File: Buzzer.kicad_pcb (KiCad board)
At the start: 4 copper layers, 70 x 90 mm, 57 parts, among them J1 AudioJack2_Ground, J2 AVR-ISP-6, J3 Screw_Terminal_01x07, J4 Screw_Terminal_01x02, J5 Screw_Terminal_01x02, J6 Screw_Terminal_01x02, J7 Screw_Terminal_01x02, J8 USB-C-Board, Q1 BC547, Q2 BC547, Q3 BC547, Q4 BC547, Q5 BC547, SW1 SW_Reset, SW2 SW_Next, SW3 SW_New, U1 ATmega328-P, U2 HDSP-7401, Y1 16 (or 20) MHz

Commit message: Add revision 2 circuit, pcb and documentation.
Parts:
- removed D6: Rot, LED_THT:LED_Rectangular_W3.9mm_H1.8mm
- removed D7: Grün, LED_THT:LED_Rectangular_W3.9mm_H1.8mm
- removed Q1, Q2, Q3, Q4, Q5: BC547, Package_TO_SOT_THT:TO-92_Inline_Wide
- added C13: 47u, Capacitor_THT:CP_Radial_D8.0mm_P3.50mm, F.Cu at (124.5, 53.3)
- added C14: 100n, Capacitor_THT:C_Disc_D5.0mm_W2.5mm_P2.50mm, F.Cu at (129.5, 97.8)
- added C15: 100n, Capacitor_THT:C_Disc_D5.0mm_W2.5mm_P2.50mm, F.Cu at (129.5, 109.2)
- added C16: 100n, Capacitor_THT:C_Disc_D5.0mm_W2.5mm_P2.50mm, F.Cu at (129.5, 120.6)
- added C17: 100n, Capacitor_THT:C_Disc_D5.0mm_W2.5mm_P2.50mm, F.Cu at (144.7, 57.0)
- added C18: 220n, Capacitor_THT:C_Disc_D5.0mm_W2.5mm_P2.50mm, F.Cu at (134.7, 57.0)
- added C19: 100n, Capacitor_THT:C_Disc_D5.0mm_W2.5mm_P2.50mm, F.Cu at (188.0, 33.0)
- added C20: 100n, Capacitor_THT:C_Disc_D5.0mm_W2.5mm_P2.50mm, F.Cu at (182.9, 35.6)
- added C21: 100n, Capacitor_THT:C_Disc_D5.0mm_W2.5mm_P2.50mm, F.Cu at (170.2, 96.5)
- added D_{Buzz}1: LED_Small, LED_THT:LED_Rectangular_W5.0mm_H2.0mm, F.Cu at (248.9, 81.3)
- added D_{Power}1: LED_Small, LED_THT:LED_Rectangular_W5.0mm_H2.0mm, F.Cu at (243.8, 81.3)
- added D_{P}1: LED_Small, LED_THT:LED_Rectangular_W5.0mm_H2.0mm, F.Cu at (203.2, 132.2)
- added D_{P}2: LED_Small, LED_THT:LED_Rectangular_W5.0mm_H2.0mm, F.Cu at (208.3, 132.2)
- added D_{P}3: LED_Small, LED_THT:LED_Rectangular_W5.0mm_H2.0mm, F.Cu at (213.4, 132.2)
- added D_{P}4: LED_Small, LED_THT:LED_Rectangular_W5.0mm_H2.0mm, F.Cu at (218.4, 132.1)
- added D_{P}5: LED_Small, LED_THT:LED_Rectangular_W5.0mm_H2.0mm, F.Cu at (223.5, 132.1)
- added D_{P}6: LED_Small, LED_THT:LED_Rectangular_W5.0mm_H2.0mm, F.Cu at (228.6, 132.1)
- added D_{RX}1: LED_Small, LED_THT:LED_Rectangular_W5.0mm_H2.0mm, F.Cu at (256.5, 81.3)
- added D_{Ready}1: LED_Small, LED_THT:LED_Rectangular_W5.0mm_H2.0mm, F.Cu at (193.0, 132.1)
- added D_{TX}1: LED_Small, LED_THT:LED_Rectangular_W5.0mm_H2.0mm, F.Cu at (261.6, 81.3)
- added G***: LOGO, LOGO, F.Cu at (259.1, 49.5)
- added G***: LOGO, LOGO, F.Cu at (241.3, 38.1)
- added G***: LOGO, LOGO, F.Cu at (165.1, 83.8)
- added G***: LOGO, LOGO, B.Cu at (223.5, 33.0)
- added J10: Barrel_Jack, Connector_BarrelJack:BarrelJack_Kycon_KLDX-0202-xC_Horizontal, F.Cu at (127.0, 42.4)
- added J11: Screw_Terminal_01x10, TerminalBlock_Phoenix:TerminalBlock_Phoenix_MKDS-1,5-10-5.08_1x10_P5.08mm_Horizontal, F.Cu at (261.6, 147.3)
- added J12: Conn_01x03_Pin, Connector_PinHeader_2.54mm:PinHeader_1x03_P2.54mm_Vertical, F.Cu at (185.4, 48.3)
- added J13: Screw_Terminal_01x03, TerminalBlock_Phoenix:TerminalBlock_Phoenix_MKDS-1,5-3-5.08_1x03_P5.08mm_Horizontal, F.Cu at (160.0, 33.0)
- added J9: USB_B, Connector_USB:USB_B_OST_USB-B1HSxx_Horizontal, F.Cu at (170.2, 43.4)
- added JP2: USB Reset, Connector_PinHeader_2.54mm:PinHeader_1x03_P2.54mm_Vertical, F.Cu at (188.0, 63.5)
- added JP3: USB-UART, Connector_PinHeader_2.54mm:PinHeader_1x03_P2.54mm_Vertical, F.Cu at (190.5, 48.3)
- added R17: 220-1k, Resistor_THT:R_Axial_DIN0207_L6.3mm_D2.5mm_P10.16mm_Horizontal, F.Cu at (218.4, 137.2)
- added R18: 220-1k, Resistor_THT:R_Axial_DIN0207_L6.3mm_D2.5mm_P10.16mm_Horizontal, F.Cu at (223.5, 137.2)
- added R19: 220-1k, Resistor_THT:R_Axial_DIN0207_L6.3mm_D2.5mm_P10.16mm_Horizontal, F.Cu at (228.6, 137.2)
- added R20: 220-1k, Resistor_THT:R_Axial_DIN0207_L6.3mm_D2.5mm_P10.16mm_Horizontal, F.Cu at (261.6, 63.5)
- added R21: 220-1k, Resistor_THT:R_Axial_DIN0207_L6.3mm_D2.5mm_P10.16mm_Horizontal, F.Cu at (256.5, 63.5)
- added R22: 220-1k, Resistor_THT:R_Axial_DIN0207_L6.3mm_D2.5mm_P10.16mm_Horizontal, F.Cu at (248.9, 63.5)
- added R23: 220-1k, Resistor_THT:R_Axial_DIN0207_L6.3mm_D2.5mm_P10.16mm_Horizontal, F.Cu at (243.8, 63.5)
- added R24: 10k, Resistor_THT:R_Axial_DIN0207_L6.3mm_D2.5mm_P7.62mm_Horizontal, F.Cu at (152.4, 86.4)
- added R25: 10k, Resistor_THT:R_Axial_DIN0207_L6.3mm_D2.5mm_P10.16mm_Horizontal, F.Cu at (147.3, 88.9)
- added R26: 10k, Resistor_THT:R_Axial_DIN0207_L6.3mm_D2.5mm_P15.24mm_Horizontal, F.Cu at (142.2, 94.0)
- added R27: 10k, Resistor_THT:R_Axial_DIN0207_L6.3mm_D2.5mm_P15.24mm_Horizontal, F.Cu at (142.2, 106.7)
- added R28: 10k, Resistor_THT:R_Axial_DIN0207_L6.3mm_D2.5mm_P10.16mm_Horizontal, F.Cu at (147.3, 111.8)
- added R29: 10k, Resistor_THT:R_Axial_DIN0207_L6.3mm_D2.5mm_P7.62mm_Horizontal, F.Cu at (152.4, 114.3)
- added R30: 10k, Resistor_THT:R_Axial_DIN0207_L6.3mm_D2.5mm_P10.16mm_Horizontal, F.Cu at (180.3, 134.6)
- added R31: 10k, Resistor_THT:R_Axial_DIN0207_L6.3mm_D2.5mm_P10.16mm_Horizontal, F.Cu at (160.0, 134.6)
- added REF**: WEEE-Logo_5.6x8mm_SilkScreen, Symbol:WEEE-Logo_5.6x8mm_SilkScreen, F.Cu at (123.8, 152.4)
- added REF**: OSHW-Symbol_6.7x6mm_SilkScreen, Symbol:OSHW-Symbol_6.7x6mm_SilkScreen, F.Cu at (132.1, 152.4)
- added REF**: MountingHole_2.7mm_M2.5_ISO7380_Pad, MountingHole:MountingHole_2.7mm_M2.5_ISO7380_Pad, F.Cu at (116.8, 31.6)
- added REF**: MountingHole_2.7mm_M2.5_ISO7380_Pad, MountingHole:MountingHole_2.7mm_M2.5_ISO7380_Pad, F.Cu at (264.1, 153.9)
- added REF**: MountingHole_2.7mm_M2.5_ISO7380_Pad, MountingHole:MountingHole_2.7mm_M2.5_ISO7380_Pad, F.Cu at (116.8, 153.9)
- added REF**: MountingHole_2.7mm_M2.5_ISO7380_Pad, MountingHole:MountingHole_2.7mm_M2.5_ISO7380_Pad, F.Cu at (264.1, 31.6)
- added REF**: Symbol_Barrel_Polarity, Symbol:Symbol_Barrel_Polarity, B.Cu at (127.0, 30.5)
- added REF**: Smolhaj_Scale_0.1, Symbol:Smolhaj_Scale_0.1, B.Cu at (266.0, 39.5)
- added U3: 74HC4051, Package_DIP:DIP-16_W7.62mm_Socket, F.Cu at (213.4, 104.1)
- added U4: 4511, Package_DIP:DIP-16_W7.62mm_Socket, F.Cu at (205.7, 53.3)
- added U5: CH340C, Package_SO:SOIC-16_3.9x9.9mm_P1.27mm, F.Cu at (189.2, 40.0)
- added U6: L7805, Package_TO_SOT_THT:TO-220-3_Horizontal_TabDown, F.Cu at (137.2, 53.3)
- added U7: 74LS07, Package_DIP:DIP-14_W7.62mm_Socket, F.Cu at (246.4, 149.9)
- added U8: 74LS07, Package_DIP:DIP-14_W7.62mm_Socket, F.Cu at (238.8, 88.9)
- C1, C4: footprint Capacitor_THT:CP_Radial_D10.0mm_P2.50mm -> Capacitor_THT:CP_Radial_D6.3mm_P2.50mm
- C10, C11, C12, C7, C8, C9: value 10n -> 100n; footprint Capacitor_THT:C_Disc_D3.0mm_W1.6mm_P2.50mm -> Capacitor_THT:C_Disc_D5.0mm_W2.5mm_P2.50mm
- C2, C3: footprint Capacitor_THT:C_Disc_D3.0mm_W1.6mm_P2.50mm -> Capacitor_THT:C_Disc_D5.0mm_W2.5mm_P5.00mm
- C5, C6: footprint Capacitor_THT:C_Disc_D3.0mm_W1.6mm_P2.50mm -> Capacitor_THT:C_Disc_D5.0mm_W2.5mm_P2.50mm
- D1, D5: value Rot -> SR104; footprint LED_THT:LED_Rectangular_W3.9mm_H1.8mm -> Diode_THT:D_DO-41_SOD81_P7.62mm_Horizontal
- D2: value BAT85 -> SR104; footprint Diode_THT:D_T-1_P5.08mm_Horizontal -> Diode_THT:D_DO-41_SOD81_P7.62mm_Horizontal
- D3: value BAT85 -> SR104; footprint Diode_THT:D_T-1_P5.08mm_Horizontal -> Diode_THT:D_DO-41_SOD81_P12.70mm_Horizontal
- D4: value Rot -> 1N4001; footprint LED_THT:LED_Rectangular_W3.9mm_H1.8mm -> Diode_THT:D_DO-41_SOD81_P7.62mm_Horizontal
- J1: value AudioJack2_Ground -> AudioJack3; footprint Connector_Audio:Jack_3.5mm_CUI_SJ1-3523N_Horizontal -> Connector_Audio:Jack_3.5mm_Ledino_KB3SPRS_Horizontal
- J3: value Screw_Terminal_01x07 -> Player 1; footprint TerminalBlock_Phoenix:TerminalBlock_Phoenix_MPT-0,5-7-2.54_1x07_P2.54mm_Horizontal -> TerminalBlock_Phoenix:TerminalBlock_Phoenix_MKDS-1,5-2-5.08_1x02_P5.08mm_Horizontal
- J4: value Screw_Terminal_01x02 -> Player 2; footprint TerminalBlock_Phoenix:TerminalBlock_Phoenix_MPT-0,5-2-2.54_1x02_P2.54mm_Horizontal -> TerminalBlock_Phoenix:TerminalBlock_Phoenix_MKDS-1,5-2-5.08_1x02_P5.08mm_Horizontal
- J5: value Screw_Terminal_01x02 -> Player 3; footprint TerminalBlock_Phoenix:TerminalBlock_Phoenix_MPT-0,5-2-2.54_1x02_P2.54mm_Horizontal -> TerminalBlock_Phoenix:TerminalBlock_Phoenix_MKDS-1,5-2-5.08_1x02_P5.08mm_Horizontal
- J6: value Screw_Terminal_01x02 -> Player 4; footprint TerminalBlock_Phoenix:TerminalBlock_Phoenix_MPT-0,5-2-2.54_1x02_P2.54mm_Horizontal -> TerminalBlock_Phoenix:TerminalBlock_Phoenix_MKDS-1,5-2-5.08_1x02_P5.08mm_Horizontal
- J7: value Screw_Terminal_01x02 -> Player 5; footprint TerminalBlock_Phoenix:TerminalBlock_Phoenix_MPT-0,5-2-2.54_1x02_P2.54mm_Horizontal -> TerminalBlock_Phoenix:TerminalBlock_Phoenix_MKDS-1,5-2-5.08_1x02_P5.08mm_Horizontal
- J8: value USB-C-Board -> Player 6; footprint Connector_PinHeader_2.54mm:PinHeader_1x06_P2.54mm_Horizontal -> TerminalBlock_Phoenix:TerminalBlock_Phoenix_MKDS-1,5-2-5.08_1x02_P5.08mm_Horizontal
- JP1: footprint Connector_PinHeader_2.54mm:PinHeader_1x02_P2.54mm_Vertical -> Connector_PinHeader_2.54mm:PinHeader_1x03_P2.54mm_Vertical
- R1, R10, R11, R2, R3, R4, R5, R6, R7, R8, R9: footprint Resistor_THT:R_Axial_DIN0204_L3.6mm_D1.6mm_P5.08mm_Horizontal -> Resistor_THT:R_Axial_DIN0207_L6.3mm_D2.5mm_P10.16mm_Horizontal
- R12: value 680 -> 10k; footprint Resistor_THT:R_Axial_DIN0204_L3.6mm_D1.6mm_P5.08mm_Horizontal -> Resistor_THT:R_Axial_DIN0207_L6.3mm_D2.5mm_P10.16mm_Horizontal
- R13, R14, R15, R16: value 680 -> 220-1k; footprint Resistor_THT:R_Axial_DIN0204_L3.6mm_D1.6mm_P5.08mm_Horizontal -> Resistor_THT:R_Axial_DIN0207_L6.3mm_D2.5mm_P10.16mm_Horizontal
- U1: value ATmega328-P -> ATmega328P-P; footprint Package_DIP:DIP-28_W7.62mm -> Package_DIP:DIP-28_W7.62mm_Socket
- U2: value HDSP-7401 -> HDSP-7803; footprint Display_7Segment:D1X8K -> Display_7Segment:HDSP-7801
- Y1: footprint Crystal:Resonator-2Pin_W7.0mm_H2.5mm -> Crystal:Crystal_HC49-U_Vertical
- moved U2 208.7 mm to (226.1, 66.0)
- moved R8 201.9 mm to (238.8, 45.7), turned to -90 degrees
- moved R4 199.2 mm to (238.8, 81.3), turned to 90 degrees
- moved R5 193.9 mm to (233.7, 81.3), turned to 90 degrees
- moved R3 193.5 mm to (233.7, 45.7), turned to -90 degrees
- moved R2 188.2 mm to (228.6, 45.7), turned to -90 degrees
- moved R7 188.0 mm to (228.6, 81.3), turned to 90 degrees
- moved R1 183.0 mm to (223.5, 45.7), turned to -90 degrees
- moved R6 182.9 mm to (223.5, 81.3), turned to 90 degrees
- moved R16 158.1 mm to (213.4, 137.2), turned to -90 degrees
- moved C5 149.9 mm to (190.5, 99.1), turned to 180 degrees
- moved R15 147.0 mm to (208.3, 137.2)
- moved SW3 147.0 mm to (184.1, 124.5), turned to -90 degrees
- moved SW1 144.1 mm to (172.7, 73.7)
- moved R14 140.6 mm to (203.2, 137.2), turned to -90 degrees
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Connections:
- net MOSI renamed Net-(J2-MOSI)
- C10 pad 1: Net-(J7-Pin_1) -> /PD4
- C7 pad 1: Net-(J4-Pin_1) -> Net-(U5-~{RTS})
- C7 pad 2: GND -> Net-(JP2-A)
- C8 pad 1: Net-(J5-Pin_1) -> /PD2
- C9 pad 1: Net-(J6-Pin_1) -> /PD3
- D1 pad 1: Net-(D1-K) -> /V_unfused
- D1 pad 2: Net-(D1-A) -> V_BARREL
- D2 pad 1: Net-(D2-K) -> /V_unfused
- D3 pad 1: Net-(D2-K) -> /V_unfused
- D4 pad 1: Net-(D4-K) -> /bjd
- D4 pad 2: SCK -> /bj
- D5 pad 1: Net-(D5-K) -> /V_unfused
- D5 pad 2: MISO -> V_SCREW
- F1 pad 1: Net-(D2-K) -> /V_unfused
- J1 pad R: (no net) -> Net-(C1-Pad2)
- J1 pad S: GND -> Net-(C1-Pad2)
- J1 pad T: Net-(C1-Pad2) -> GND
- J2 pad 1: MISO -> Net-(J2-MISO)
- J2 pad 3: SCK -> SCK / Buzzer
- J3 pad 1: +5V -> /PD2
- J3 pad 2: Net-(J3-Pin_2) -> GND
- J4 pad 1: Net-(J4-Pin_1) -> /PD3
- J5 pad 1: Net-(J5-Pin_1) -> /PD4
- J6 pad 1: Net-(J6-Pin_1) -> /PD5
- J7 pad 1: Net-(J7-Pin_1) -> /PD6
- J8 pad 1: unconnected-(J8-Pin_1-Pad1) -> /PD7
- J8 pad 2: unconnected-(J8-Pin_2-Pad2) -> GND
- R1 pad 1: Net-(U1-PD0) -> Net-(U4-Qa)
- R12 pad 1: Net-(D1-K) -> +5V
- R12 pad 2: Net-(Q1-B) -> RESET
- R13 pad 1: Net-(D4-K) -> Net-(D_{Ready}1-K)
- R13 pad 2: Net-(Q2-B) -> GND
- R14 pad 1: Net-(D5-K) -> Net-(D_{P}1-K)
- R14 pad 2: Net-(Q3-B) -> GND
- R15 pad 2: Net-(Q4-B) -> GND
- R16 pad 2: Net-(Q5-B) -> GND
- R2 pad 1: Net-(U1-PD1) -> Net-(U4-Qb)
- R3 pad 1: Net-(U1-PD2) -> Net-(U4-Qc)
- R4 pad 1: Net-(U1-PD3) -> Net-(U4-Qd)
- R4 pad 2: Net-(U2-DP) -> Net-(U2-D)
- R5 pad 1: Net-(U1-PD4) -> Net-(U4-Qe)
- R5 pad 2: Net-(U2-F) -> Net-(U2-E)
- R6 pad 1: Net-(U1-PD5) -> Net-(U4-Qf)
- R6 pad 2: Net-(U2-D) -> Net-(U2-F)
- R7 pad 1: Net-(U1-PD6) -> Net-(U4-Qg)
- R7 pad 2: Net-(U2-E) -> Net-(U2-G)
- R8 pad 1: Net-(U1-PD7) -> +5V
- R8 pad 2: Net-(U2-G) -> Net-(U2-DP)
- U1 pad 11: Net-(U1-PD5) -> /PD5
- U1 pad 12: Net-(U1-PD6) -> /PD6
- U1 pad 13: Net-(U1-PD7) -> /PD7
- U1 pad 15: Audio -> New
- U1 pad 16: Net-(D1-A) -> Audio
- U1 pad 18: MISO -> Net-(J2-MISO)
- U1 pad 19: SCK -> SCK / Buzzer
- U1 pad 2: Net-(U1-PD0) -> RX
- U1 pad 23: Net-(D7-A) -> /PC0
- U1 pad 24: Net-(J4-Pin_1) -> /PC1
- U1 pad 25: Net-(J5-Pin_1) -> /PC2
- U1 pad 26: Net-(J6-Pin_1) -> /PC3
- U1 pad 27: Net-(J7-Pin_1) -> /PC4
- U1 pad 28: New -> /PC5
- U1 pad 3: Net-(U1-PD1) -> TX
- U1 pad 4: Net-(U1-PD2) -> /PD2
- U1 pad 5: Net-(U1-PD3) -> /PD3
- U1 pad 6: Net-(U1-PD4) -> /PD4
- U2 pad 1: +5V -> GND
- U2 pad 6: +5V -> GND
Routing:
- net +5V: track 160.5 -> 577.2 mm, vias 8 -> 4
- net GND: track 357.1 -> 8.02 mm, vias 13 -> 0
- net TX: track 0.00 -> 190.1 mm, vias 0 -> 2
- net RX: track 0.00 -> 168.8 mm, vias 0 -> 2
- net SCK / Buzzer: track 0.00 -> 142.7 mm, vias 0 -> 1
- net /P0: track 0.00 -> 134.5 mm, vias 0 -> 2
- net /P2: track 0.00 -> 114.6 mm, vias 0 -> 3
- net /P1: track 0.00 -> 111.6 mm, vias 0 -> 2
- net /P3: track 0.00 -> 99.1 mm, vias 0 -> 2
- net Net-(J2-MISO): track 0.00 -> 81.1 mm, vias 0 -> 1
- net /PD2: track 0.00 -> 74.8 mm
- net /P5: track 0.00 -> 74.5 mm, vias 0 -> 1
- net /PD5: track 0.00 -> 69.8 mm
- net /PD3: track 0.00 -> 66.7 mm
- net /P4: track 0.00 -> 65.8 mm, vias 0 -> 1
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- added copper zone on B.Cu, net GND
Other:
- board size 70 x 90 mm -> 155 x 130 mm
- copper layers 4 -> 2
- board text added: "+"
- board text added: "+ -"
- board text added: "-"
- board text added: "1"
- board text added: "2"
- board text added: "3"
- board text added: "4"
- board text added: "5"
- board text added: "5V"
- board text added: "5V 200mA"
- board text added: "5V OUT"
- board text added: "6"
- board text added: "8-25V"
- board text added: "8-25V 200mA"
- board text added: "Active player output (open collector)"
- board text added: "Boop!"
- board text added: "Buzzer"
- board text added: "CH340"
- board text added: "CH340 USB-UART"
- board text added: "HAJ"
- board text added: "Kein Platz für Rassismus!"
- board text added: "Lieber queer und lebensfroh, als verklemmt und hetero!"
- board text added: "New Game"
- board text added: "Next place"
- board text added: "OFF ON"
- board text added: "ON OFF"
- board text added: "OwO, what's this?"
- board text added: "P1"
- board text added: "P2"
- board text added: "P3"
- board text added: "P4"
- board text added: "P6"
- board text added: "Power"
- board text added: "Quiz Buzzer Revision 2 github.com/Port39/quizbuzzer"
- board text added: "RX (Device->uC)"
- board text added: "Ready"
- board text added: "Speaker"
- board text added: "TX (uC->Device)"
- board text added: "TX RX GND"
- board text added: "USB-Reset"

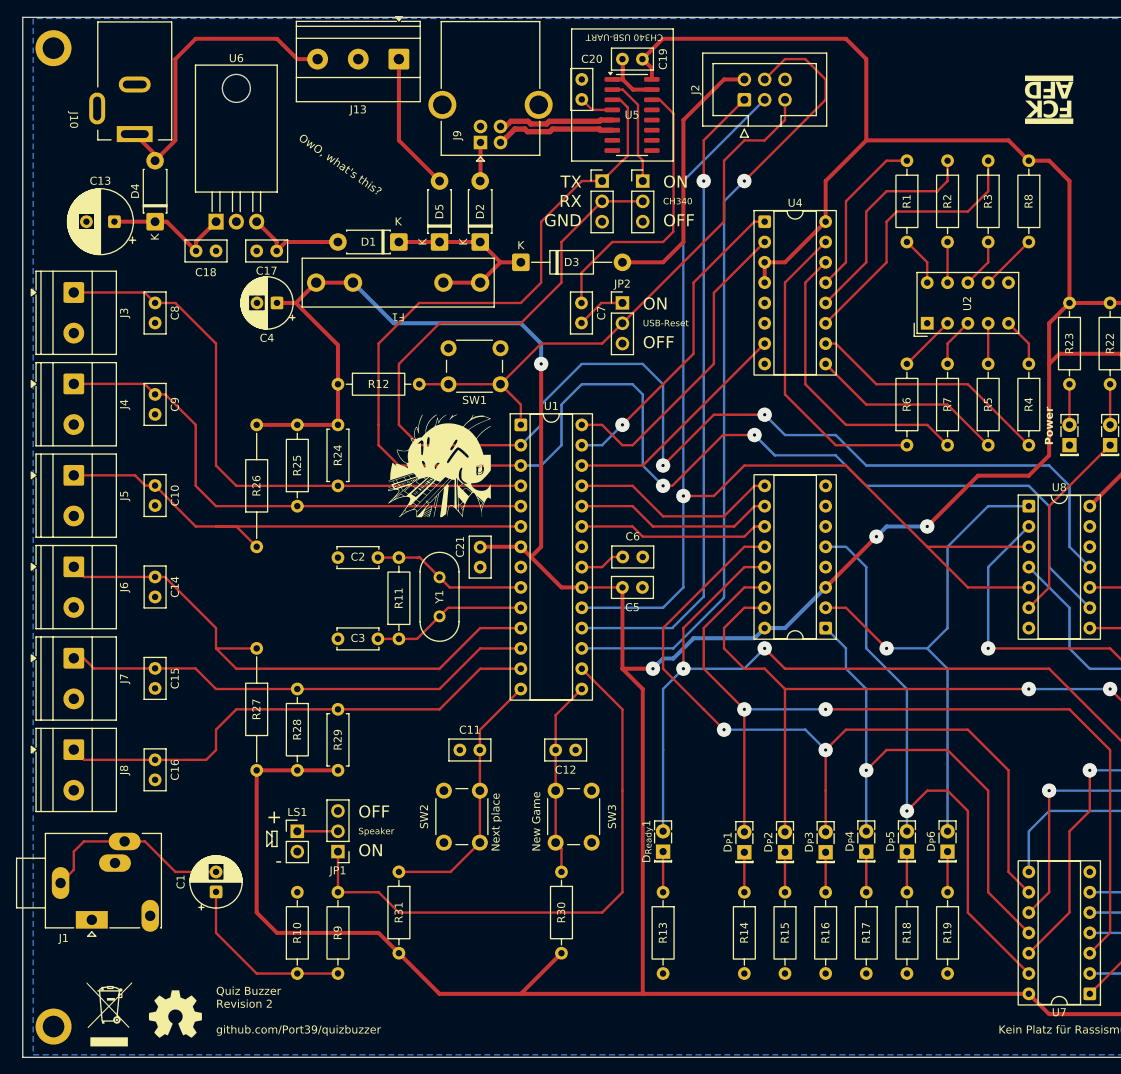
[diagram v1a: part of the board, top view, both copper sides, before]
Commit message: Set schematic revisions by variables.
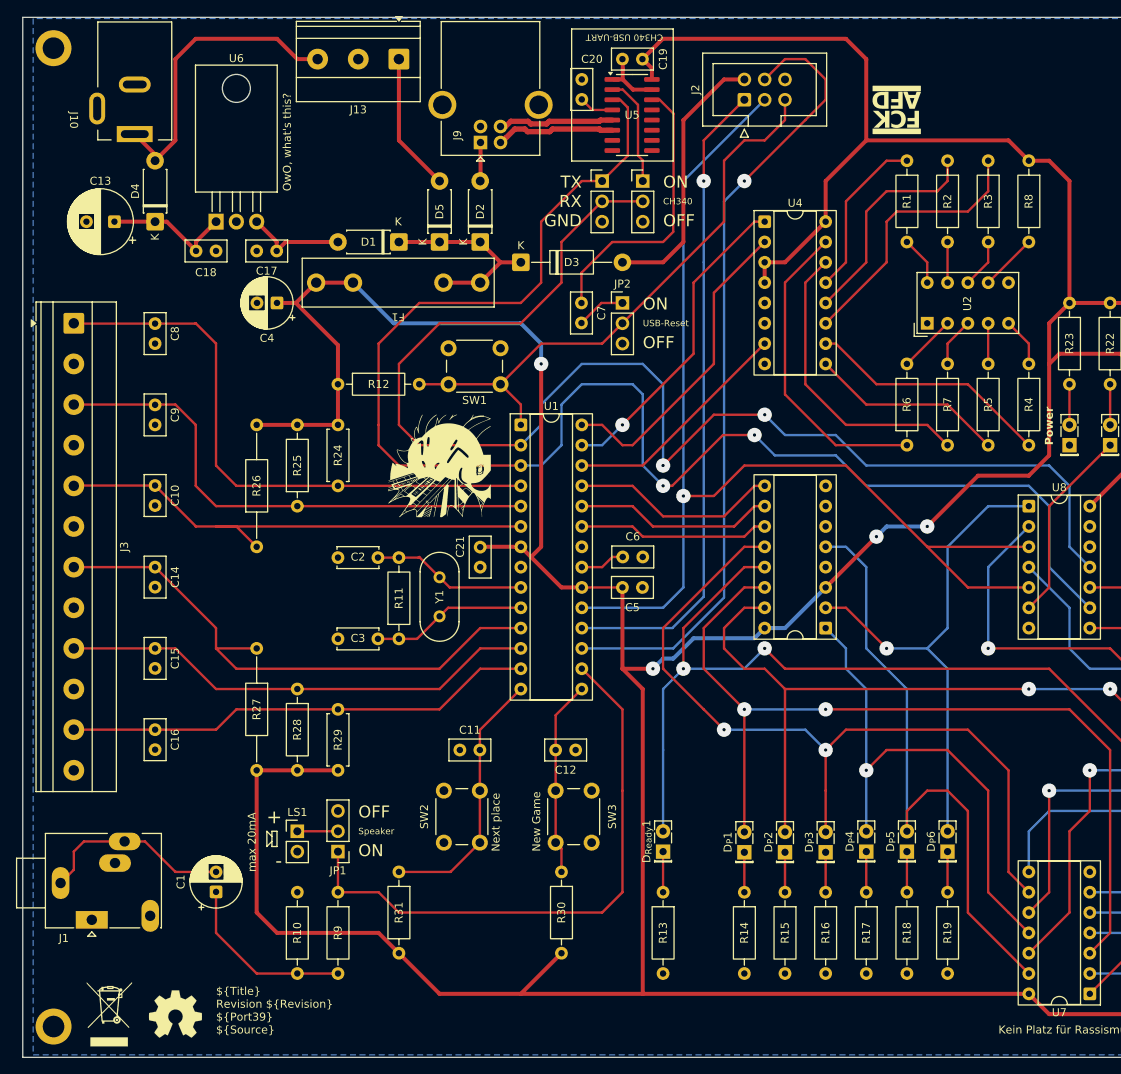
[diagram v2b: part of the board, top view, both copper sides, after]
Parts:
- removed J4: Player 2, TerminalBlock_Phoenix:TerminalBlock_Phoenix_MKDS-1,5-2-5.08_1x02_P5.08mm_Horizontal
- removed J5: Player 3, TerminalBlock_Phoenix:TerminalBlock_Phoenix_MKDS-1,5-2-5.08_1x02_P5.08mm_Horizontal
- removed J6: Player 4, TerminalBlock_Phoenix:TerminalBlock_Phoenix_MKDS-1,5-2-5.08_1x02_P5.08mm_Horizontal
- removed J7: Player 5, TerminalBlock_Phoenix:TerminalBlock_Phoenix_MKDS-1,5-2-5.08_1x02_P5.08mm_Horizontal
- removed J8: Player 6, TerminalBlock_Phoenix:TerminalBlock_Phoenix_MKDS-1,5-2-5.08_1x02_P5.08mm_Horizontal
- J3: value Player 1 -> Screw_Terminal_01x12; footprint TerminalBlock_Phoenix:TerminalBlock_Phoenix_MKDS-1,5-2-5.08_1x02_P5.08mm_Horizontal -> TerminalBlock_Phoenix:TerminalBlock_Phoenix_MKDS-1,5-12-5.08_1x12_P5.08mm_Horizontal
- moved G*** 19.1 mm to (222.2, 39.4)
- moved J3 3.85 mm to (119.4, 66.0)
- moved C16 3.77 mm to (129.5, 116.8)
- moved C8 2.58 mm to (129.5, 66.1)
- moved C15 2.50 mm to (129.5, 106.7)
- moved G*** 1.80 mm to (222.2, 31.8)
- moved C9 1.31 mm to (129.5, 76.2)
- moved C14 1.23 mm to (129.5, 96.5)
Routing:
- net /PD7: track 62.6 -> 59.0 mm
- net /P5: track 74.5 -> 77.0 mm, vias 1 -> 0
- net /PD2: track 74.8 -> 73.3 mm
- net /PD3: track 66.7 -> 65.6 mm
- net /PD6: track 59.6 -> 60.1 mm
- net /PD4: track 64.7 -> 64.2 mm
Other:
- board text added: "${Title} Revision ${Revision} ${Port39} ${Source}"
- board text added: "P5"
- board text added: "max 20mA"
- board text removed: "Quiz Buzzer Revision 2 github.com/Port39/quizbuzzer"
